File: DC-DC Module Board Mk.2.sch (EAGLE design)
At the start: 145 parts, among them U1 PCA9685, U3 LM1085IS-5.0

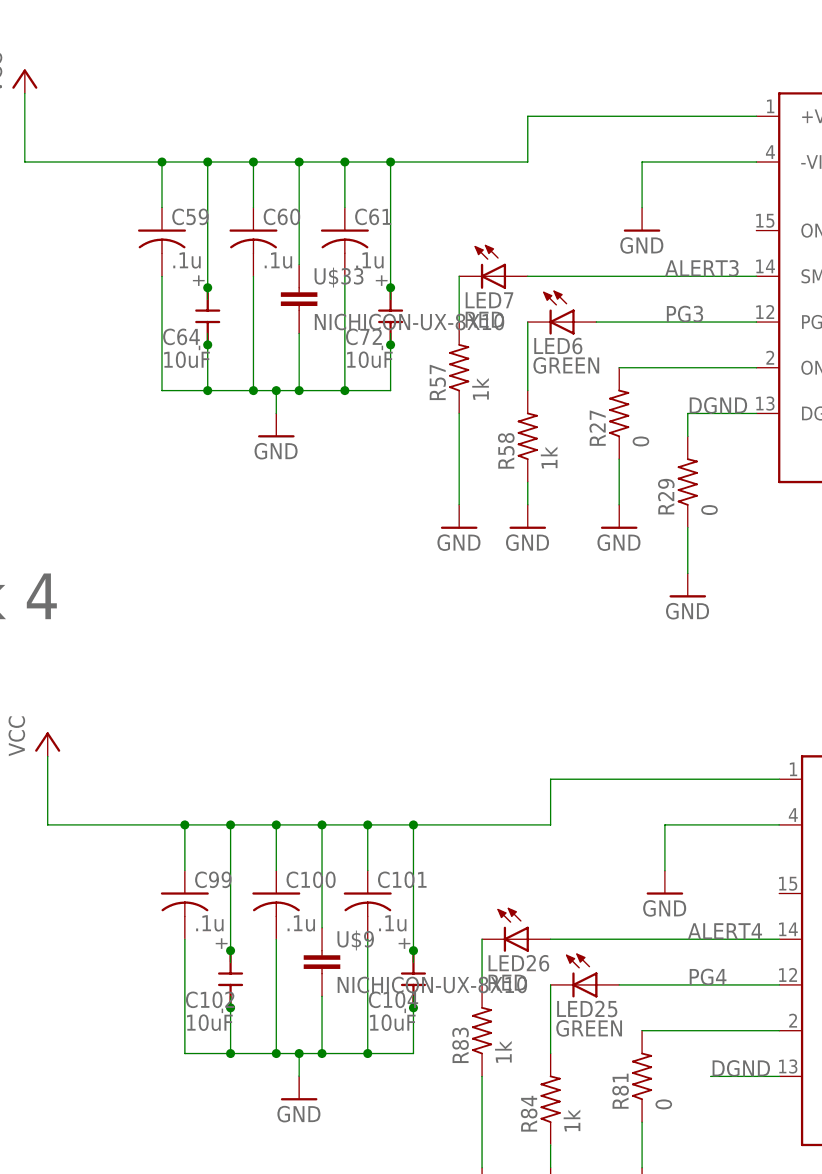
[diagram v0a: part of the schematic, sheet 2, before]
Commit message: fixed cap, named boards and caps
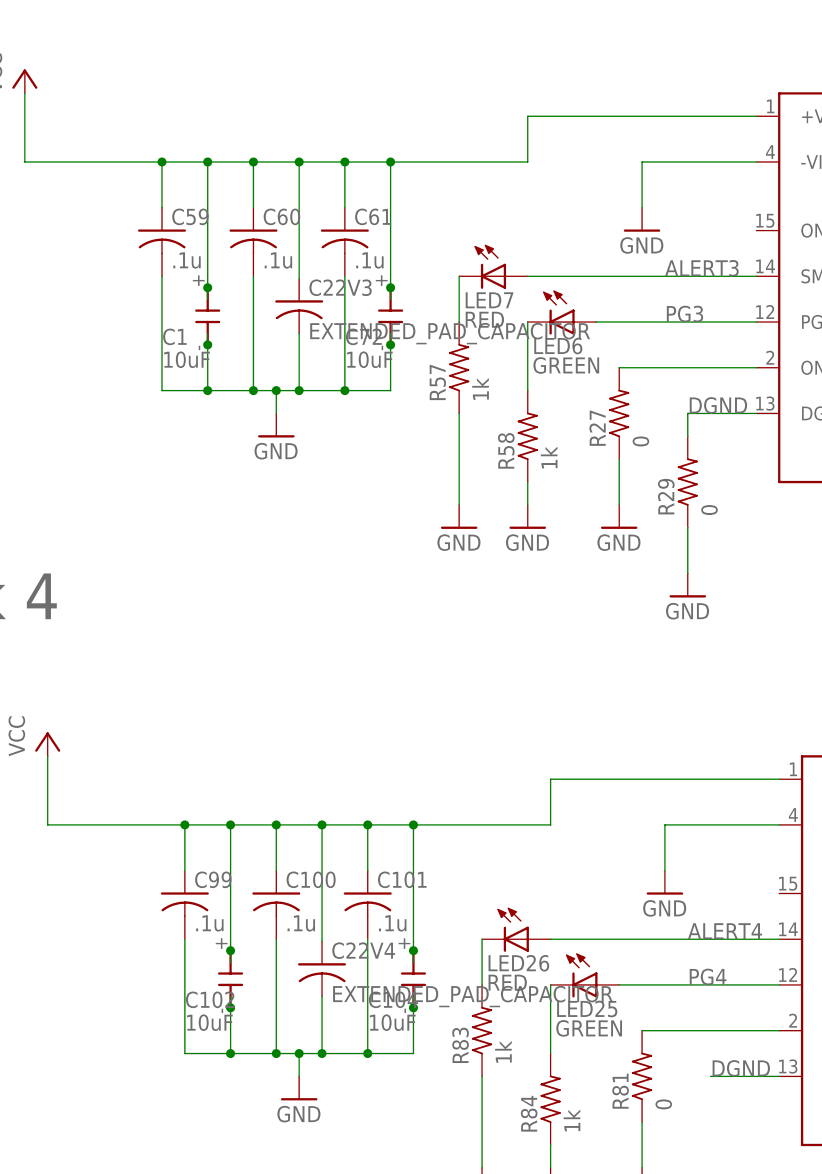
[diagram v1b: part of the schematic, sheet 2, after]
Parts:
- removed U$33, U$5, U$6, U$9: NICHICON-UX-8X10, ExtendedPadCap:NICHICON-UX-8X10
- added C22V1, C22V2, C22V3, C22V4: EXTENDED_PAD_CAPACITOR, ExtendedPadCap:EXTENDED_PAD_CAPACITOR
- renumbered C64 to C1, U$1 to BRICK1, U$14 to BRICK3, U$22 to BRICK2, U$42 to BRICK4
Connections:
- net +48V: now also C22V1.3, C22V2.3, C22V3.3, C22V4.3; no longer U$33.1, U$5.1, U$6.1, U$9.1
- net GND: now also C22V1.4, C22V2.4, C22V3.4, C22V4.4; no longer U$33.2, U$5.2, U$6.2, U$9.2

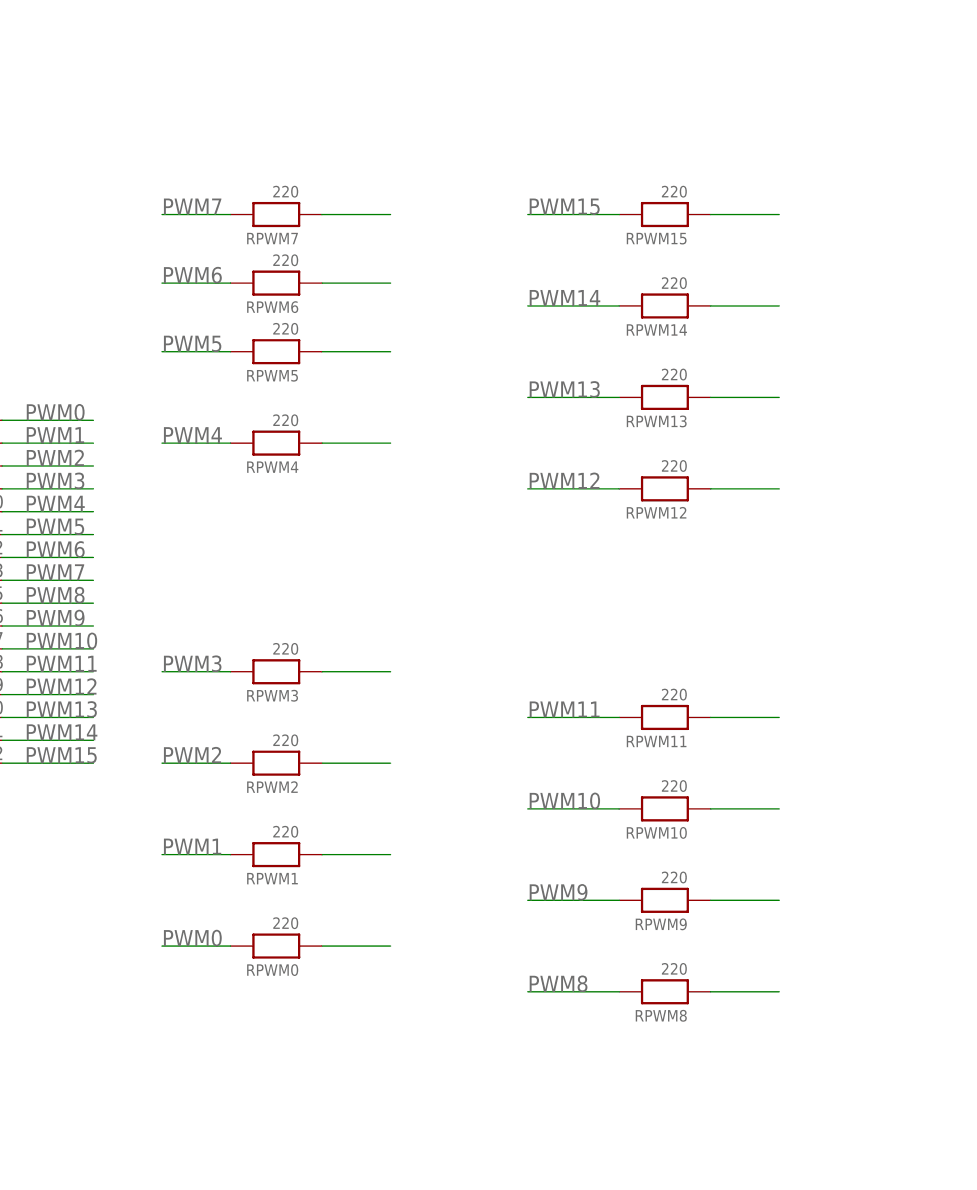
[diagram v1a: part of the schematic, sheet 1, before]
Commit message: changed names of connectors, added header pins for pwm chip
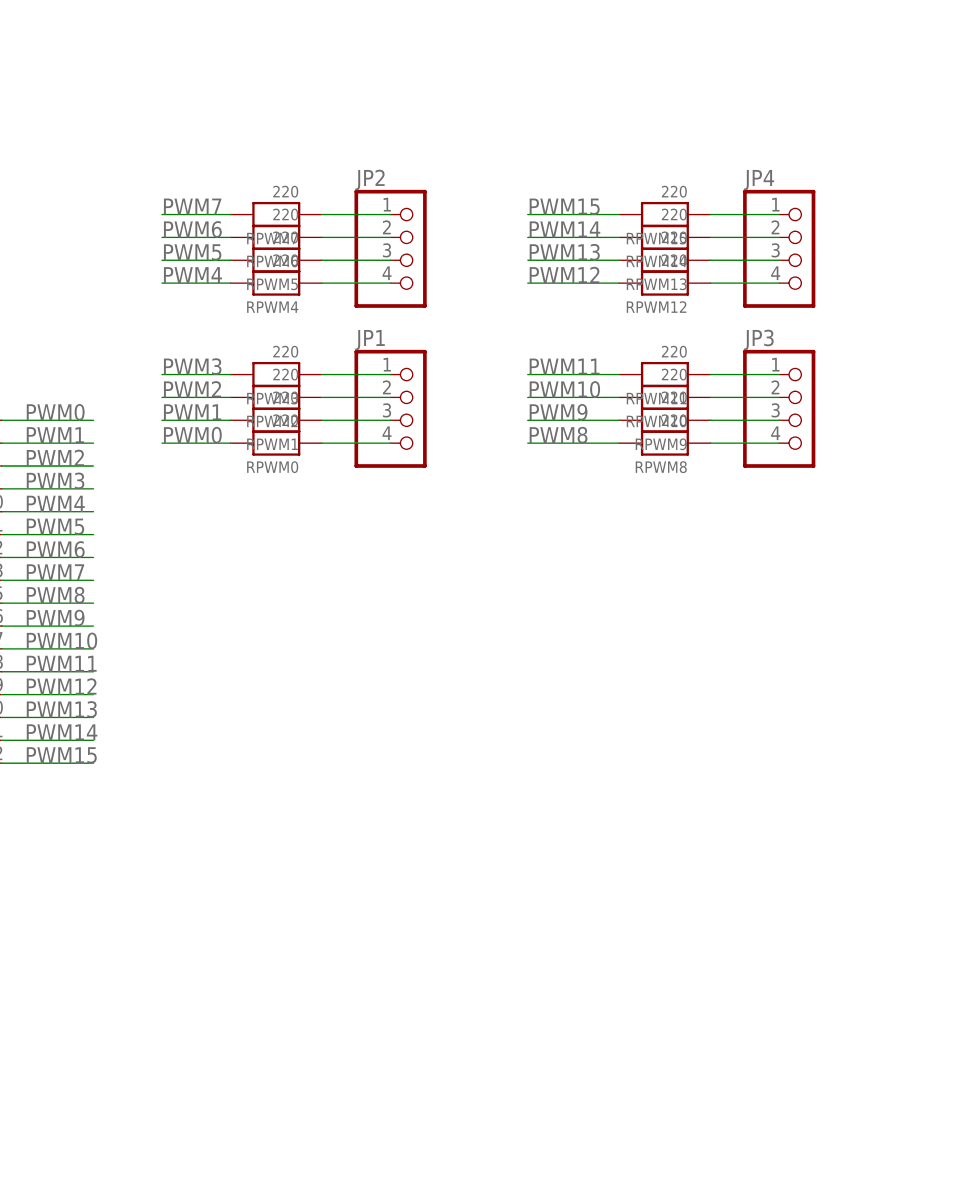
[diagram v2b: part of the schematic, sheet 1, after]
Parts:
- added JP1, JP2, JP3, JP4: (no value), pinhead:PINHD-1X4
- renumbered U$15 to UFIT0, U$20 to UFIT1, U$23 to UFIT6, U$24 to UFIT5, U$25 to UFIT4, U$26 to UFIT3, U$27 to UFIT7, U$28 to UFIT8, U$29 to UFITTUBE, U$30 to UFIT2, U$31 to UFITCAN
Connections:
- net N$14: now also JP2.2
- net N$20: now also JP2.1
- net N$21: now also JP2.3
- net N$24: now also JP2.4
- net N$26: now also JP1.1
- net N$27: now also JP1.2
- net N$28: now also JP1.3
- net N$29: now also JP1.4
- net N$30: now also JP3.4
- net N$31: now also JP3.3
- net N$32: now also JP3.2
- net N$37: now also JP3.1
- net N$38: now also JP4.4
- net N$39: now also JP4.3
- net N$40: now also JP4.2
- net N$41: now also JP4.1
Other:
- moved on the sheet: RPWM0, RPWM1, RPWM10, RPWM11, RPWM12, RPWM13, RPWM14, RPWM2, RPWM3, RPWM4, RPWM5, RPWM6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

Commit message: replaced ~50% of molex microfit connectors
replaced with vertical variant
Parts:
- UFIT0, UFIT2, UFIT4, UFIT6, UFIT8, UFITTUBE: value MICRO-FIT-4-SMD-HZ -> MICRO-FIT-4-SMD-HZVT; device Connectors:MICRO-FIT-4-SMD-HZ -> Connectors:MICRO-FIT-4-SMD-HZVT
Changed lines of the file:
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@@
 <grid distance="0.1" unitdist="inch" unit="inch" style="lines" multiple="1" display="no" altdistance="0.01" altunitdist="inch" altunit="inch"/>
 <layers>
-<layer number="1" name="Top" color="4" fill="1" visible="no" active="no"/>
-<layer number="2" name="Route2" color="1" fill="3" visible="no" active="no"/>
-<layer number="3" name="Route3" color="4" fill="3" visible="no" active="no"/>
-<layer number="4" name="Route4" color="1" fill="4" visible="no" active="no"/>
-<layer number="5" name="Route5" color="4" fill="4" visible="no" active="no"/>
-<layer number="6" name="Route6" color="1" fill="8" visible="no" active="no"/>
-<layer number="7" name="Route7" color="4" fill="8" visible="no" active="no"/>
-<layer number="8" name="Route8" color="1" fill="2" visible="no" active="no"/>
-<layer number="9" name="Route9" color="4" fill="2" visible="no" active="no"/>
-<layer number="10" name="Route10" color="1" fill="7" visible="no" active="no"/>
-<layer number="11" name="Route11" color="4" fill="7" visible="no" active="no"/>
-<layer number="12" name="Route12" color="1" fill="5" visible="no" active="no"/>
-<layer number="13" name="Route13" color="4" fill="5" visible="no" active="no"/>
-<layer number="14" name="Route14" color="1" fill="6" visible="no" active="no"/>
-<layer number="15" name="Route15" color="4" fill="6" visible="no" active="no"/>
-<layer number="16" name="Bottom" color="1" fill="1" visible="no" active="no"/>
-<layer number="17" name="Pads" color="2" fill="1" visible="no" active="no"/>
-<layer number="18" name="Vias" color="2" fill="1" visible="no" active="no"/>
-<layer number="19" name="Unrouted" color="6" fill="1" visible="no" active="no"/>
-<layer number="20" name="Dimension" color="15" fill="1" visible="no" active="no"/>
-<layer number="21" name="tPlace" color="7" fill="1" visible="no" active="no"/>
-<layer number="22" name="bPlace" color="13" fill="1" visible="no" active="no"/>
-<layer number="23" name="tOrigins" color="15" fill="1" visible="no" active="no"/>
-<layer number="24" name="bOrigins" color="13" fill="1" visible="no" active="no"/>
-<layer number="25" name="tNames" color="7" fill="1" visible="no" active="no"/>
-<layer number="26" name="bNames" color="7" fill="1" visible="no" active="no"/>
-<layer number="27" name="tValues" color="7" fill="1" visible="no" active="no"/>
-<layer number="28" name="bValues" color="7" fill="1" visible="no" active="no"/>
+<layer number="1" name="Top" color="4" fill="1" visible="yes" active="no"/>
+<layer number="2" name="Route2" color="1" fill="3" visible="yes" active="no"/>
+<layer number="3" name="Route3" color="4" fill="3" visible="yes" active="no"/>
+<layer number="4" name="Route4" color="1" fill="4" visible="yes" active="no"/>
+<layer number="5" name="Route5" color="4" fill="4" visible="yes" active="no"/>
+<layer number="6" name="Route6" color="1" fill="8" visible="yes" active="no"/>
+<layer number="7" name="Route7" color="4" fill="8" visible="yes" active="no"/>
+<layer number="8" name="Route8" color="1" fill="2" visible="yes" active="no"/>
+<layer number="9" name="Route9" color="4" fill="2" visible="yes" active="no"/>
+<layer number="10" name="Route10" color="1" fill="7" visible="yes" active="no"/>
+<layer number="11" name="Route11" color="4" fill="7" visible="yes" active="no"/>
+<layer number="12" name="Route12" color="1" fill="5" visible="yes" active="no"/>
+<layer number="13" name="Route13" color="4" fill="5" visible="yes" active="no"/>
+<layer number="14" name="Route14" color="1" fill="6" visible="yes" active="no"/>
+<layer number="15" name="Route15" color="4" fill="6" visible="yes" active="no"/>
+<layer number="16" name="Bottom" color="1" fill="1" visible="yes" active="no"/>
+<layer number="17" name="Pads" color="2" fill="1" visible="yes" active="no"/>
+<layer number="18" name="Vias" color="2" fill="1" visible="yes" active="no"/>
+<layer number="19" name="Unrouted" color="6" fill="1" visible="yes" active="no"/>
+<layer number="20" name="Dimension" color="15" fill="1" visible="yes" active="no"/>
+<layer number="21" name="tPlace" color="7" fill="1" visible="yes" active="no"/>
+<layer number="22" name="bPlace" color="13" fill="1" visible="yes" active="no"/>
+<layer number="23" name="tOrigins" color="15" fill="1" visible="yes" active="no"/>
+<layer number="24" name="bOrigins" color="13" fill="1" visible="yes" active="no"/>
+<layer number="25" name="tNames" color="7" fill="1" visible="yes" active="no"/>
+<layer number="26" name="bNames" color="7" fill="1" visible="yes" active="no"/>
+<layer number="27" name="tValues" color="7" fill="1" visible="yes" active="no"/>
+<layer number="28" name="bValues" color="7" fill="1" visible="yes" active="no"/>
 <layer number="29" name="tStop" color="7" fill="3" visible="no" active="no"/>
 <layer number="30" name="bStop" color="7" fill="6" visible="no" active="no"/>
@@
 <layer number="35" name="tGlue" color="7" fill="4" visible="no" active="no"/>
 <layer number="36" name="bGlue" color="7" fill="5" visible="no" active="no"/>
-<layer number="37" name="tTest" color="7" fill="1" visible="no" active="no"/>
-<layer number="38" name="bTest" color="7" fill="1" visible="no" active="no"/>
+<layer number="37" name="tTest" color="7" fill="1" visible="yes" active="no"/>
+<layer number="38" name="bTest" color="7" fill="1" visible="yes" active="no"/>
 <layer number="39" name="tKeepout" color="4" fill="11" visible="no" active="no"/>
 <layer number="40" name="bKeepout" color="1" fill="11" visible="no" active="no"/>
@@
 <layer number="44" name="Drills" color="7" fill="1" visible="no" active="no"/>
 <layer number="45" name="Holes" color="7" fill="1" visible="no" active="no"/>
-<layer number="46" name="Milling" color="3" fill="1" visible="no" active="no"/>
-<layer number="47" name="Measures" color="7" fill="1" visible="no" active="no"/>
-<layer number="48" name="Document" color="7" fill="1" visible="no" active="no"/>
-<layer number="49" name="Reference" color="7" fill="1" visible="no" active="no"/>
-<layer number="50" name="dxf" color="7" fill="1" visible="no" active="no"/>
-<layer number="51" name="tDocu" color="14" fill="1" visible="no" active="no"/>
-<layer number="52" name="bDocu" color="7" fill="1" visible="no" active="no"/>
-<layer number="53" name="tGND_GNDA" color="7" fill="9" visible="no" active="no"/>
-<layer number="54" name="bGND_GNDA" color="1" fill="9" visible="no" active="no"/>
-<layer number="56" name="wert" color="7" fill="1" visible="no" active="no"/>
-<layer number="57" name="tCAD" color="7" fill="1" visible="no" active="no"/>
-<layer number="59" name="tCarbon" color="7" fill="1" visible="no" active="no"/>
-<layer number="60" name="bCarbon" color="7" fill="1" visible="no" active="no"/>
+<layer number="46" name="Milling" color="3" fill="1" visible="yes" active="no"/>
+<layer number="47" name="Measures" color="7" fill="1" visible="yes" active="no"/>
+<layer number="48" name="Document" color="7" fill="1" visible="yes" active="no"/>
+<layer number="49" name="Reference" color="7" fill="1" visible="yes" active="no"/>
+<layer number="50" name="dxf" color="7" fill="1" visible="yes" active="no"/>
+<layer number="51" name="tDocu" color="14" fill="1" visible="yes" active="no"/>
+<layer number="52" name="bDocu" color="7" fill="1" visible="yes" active="no"/>
+<layer number="53" name="tGND_GNDA" color="7" fill="9" visible="yes" active="no"/>
+<layer number="54" name="bGND_GNDA" color="1" fill="9" visible="yes" active="no"/>
+<layer number="56" name="wert" color="7" fill="1" visible="yes" active="no"/>
+<layer number="57" name="tCAD" color="7" fill="1" visible="yes" active="no"/>
+<layer number="59" name="tCarbon" color="7" fill="1" visible="yes" active="no"/>
+<layer number="60" name="bCarbon" color="7" fill="1" visible="yes" active="no"/>
 <layer number="90" name="Modules" color="5" fill="1" visible="yes" active="yes"/>
 <layer number="91" name="Nets" color="2" fill="1" visible="yes" active="yes"/>
@@
 </part>
 <part name="GND39" library="supply1" deviceset="GND" device=""/>
-<part name="UFIT0" library="Connectors" deviceset="MICRO-FIT-4-SMD-HZ" device=""/>
+<part name="UFIT0" library="Connectors" deviceset="MICRO-FIT-4-SMD-HZ" device="VT" value="MICRO-FIT-4-SMD-HZVT"/>
 <part name="UFIT1" library="Connectors" deviceset="MICRO-FIT-4-SMD-HZ" device=""/>
-<part name="UFIT6" library="Connectors" deviceset="MICRO-FIT-4-SMD-HZ" device=""/>
+<part name="UFIT6" library="Connectors" deviceset="MICRO-FIT-4-SMD-HZ" device="VT" value="MICRO-FIT-4-SMD-HZVT"/>
 <part name="UFIT5" library="Connectors" deviceset="MICRO-FIT-4-SMD-HZ" device=""/>
-<part name="UFIT4" library="Connectors" deviceset="MICRO-FIT-4-SMD-HZ" device=""/>
+<part name="UFIT4" library="Connectors" deviceset="MICRO-FIT-4-SMD-HZ" device="VT" value="MICRO-FIT-4-SMD-HZVT"/>
 <part name="UFIT3" library="Connectors" deviceset="MICRO-FIT-4-SMD-HZ" device=""/>
 <part name="UFIT7" library="Connectors" deviceset="MICRO-FIT-4-SMD-HZ" device=""/>
-<part name="UFIT8" library="Connectors" deviceset="MICRO-FIT-4-SMD-HZ" device=""/>
-<part name="UFITTUBE" library="Connectors" deviceset="MICRO-FIT-4-SMD-HZ" device=""/>
-<part name="UFIT2" library="Connectors" deviceset="MICRO-FIT-4-SMD-HZ" device=""/>
+<part name="UFIT8" library="Connectors" deviceset="MICRO-FIT-4-SMD-HZ" device="VT" value="MICRO-FIT-4-SMD-HZVT"/>
+<part name="UFITTUBE" library="Connectors" deviceset="MICRO-FIT-4-SMD-HZ" device="VT" value="MICRO-FIT-4-SMD-HZVT"/>
+<part name="UFIT2" library="Connectors" deviceset="MICRO-FIT-4-SMD-HZ" device="VT" value="MICRO-FIT-4-SMD-HZVT"/>
 <part name="R22" library="rcl" deviceset="R-US_" device="R0603" value="120"/>
 <part name="R17" library="rcl" deviceset="R-US_" device="R0603" value="120"/>
